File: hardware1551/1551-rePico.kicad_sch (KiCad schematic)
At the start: 25 parts, among them J1 0.96_I2C_OLED, J10 TCBM, J11 JTAG, J6 Conn_01x05, J8 SD CARD, U1 Pico, U3 XC9572XL-VQ64, U4 6523 (pins), U5 6510T (pins), U6 6510T (socket for chip)

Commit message: board for 1551 with correct dimensions and spacing between CPU and TPI, routed
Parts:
- C1, J1, J11, J8, SWDBG1, U1, U4, U5, U6: now left out of the parts list
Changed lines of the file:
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@@
 		(unit 1)
 		(exclude_from_sim no)
-		(in_bom yes)
+		(in_bom no)
 		(on_board yes)
 		(dnp no)
@@
 		(unit 1)
 		(exclude_from_sim no)
-		(in_bom yes)
+		(in_bom no)
 		(on_board yes)
 		(dnp no)
@@
 		(unit 1)
 		(exclude_from_sim no)
-		(in_bom yes)
+		(in_bom no)
 		(on_board yes)
 		(dnp no)
@@
 		(unit 1)
 		(exclude_from_sim no)
-		(in_bom yes)
+		(in_bom no)
 		(on_board yes)
 		(dnp no)
@@
 		(unit 1)
 		(exclude_from_sim no)
-		(in_bom yes)
+		(in_bom no)
 		(on_board yes)
 		(dnp no)
@@
 		(unit 1)
 		(exclude_from_sim no)
-		(in_bom yes)
+		(in_bom no)
 		(on_board yes)
 		(dnp no)
@@
 		(unit 1)
 		(exclude_from_sim no)
-		(in_bom yes)
+		(in_bom no)
 		(on_board yes)
 		(dnp no)
@@
 		(unit 1)
 		(exclude_from_sim no)
-		(in_bom yes)
+		(in_bom no)
 		(on_board yes)
 		(dnp no)
@@
 		(unit 1)
 		(exclude_from_sim no)
-		(in_bom yes)
+		(in_bom no)
 		(on_board yes)
 		(dnp no)

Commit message: jumpers for future GPIO0/GPIO3 experiments
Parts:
- added JP2, JP5, JP6, JP7: SolderJumper_3_Bridged12, Jumper:SolderJumper-3_P1.3mm_Bridged12_RoundedPad1.0x1.5mm_NumberLabels, symbol Jumper:SolderJumper_3_Bridged12
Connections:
- net +3V3: now also JP7.3 (B)
- net DEVNUM_3V3: now also JP5.2 (C); no longer U1.5 (GPIO3)
- net GND: now also JP7.1 (A)
- net PHI0: now also JP2.2 (C); no longer U5.2 (ϕ0)
- net ~{IRQ}: now also JP6.2 (C); no longer U5.3 (~{IRQ})
- net at U1.1 (GPIO0): now also JP2.3 (B)
- new net: JP5.1 (A), JP6.3 (B), U1.5 (GPIO3)
- new net: JP5.3 (B), JP7.2 (C)
- new net PHI0_BRD: JP2.1 (A), U5.2 (ϕ0)
- new net ~{IRQ_BRD}: JP6.1 (A), U5.3 (~{IRQ})
- no-connect marks 23 -> 22
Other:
- note added: "DEFAULT - use GPIO3 to drive DEVNUM_3V3 (Pico sets device number) - IRQ comes from the board OR - swap both JP5/JP6 - IRQ comes from GPIO3 - DEVNUM_3V3 set by JP7: GND (default) is #8, +3V3 is #9"
- note added: "Pico firmware TODO: - GPIO0: SOE not used (always high), can be fixed in firmware to true OR can be used to test 2MHz clock (PHI0) for 6502 - GPIO3: Pico decides about device number - 0 or 1 OR can be used to test 100Hz (IRQ) for 6502 - GPIO5: switch driver from high/low to hi-z/low"
- note removed: "Pico firmware TODO: - GPIO0: SOE not used (always high), can be fixed in firmware to true - GPIO3: Pico decides about device number - 0 or 1 - GPIO5: switch driver from high/low to hi-z/low"

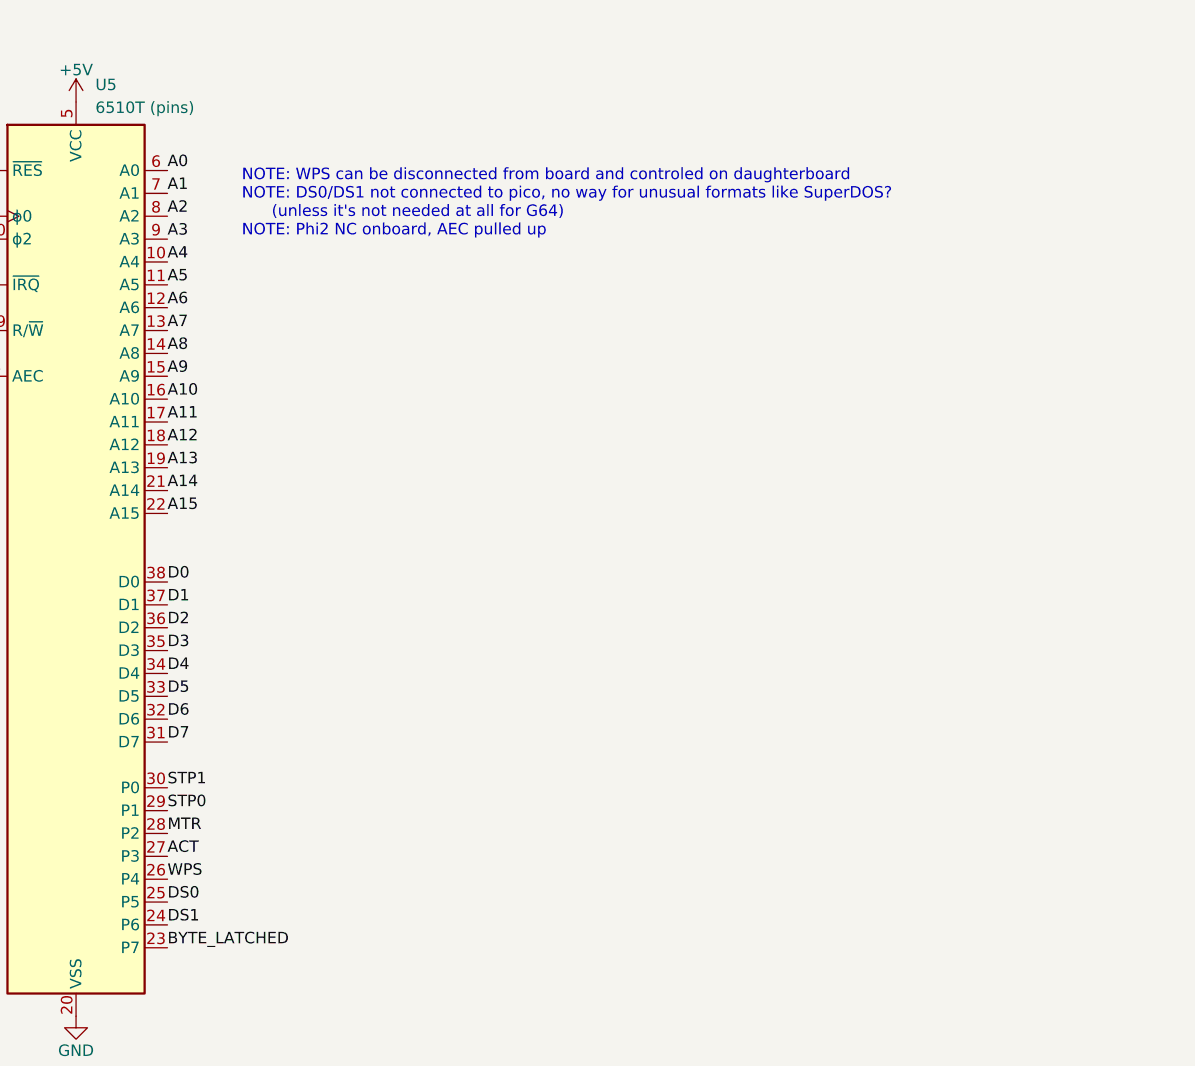
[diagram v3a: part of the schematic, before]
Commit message: disconnect WPS from mainboard WPS becuase it's an output of U8 (pin2) that will keep it low with no mechanism present
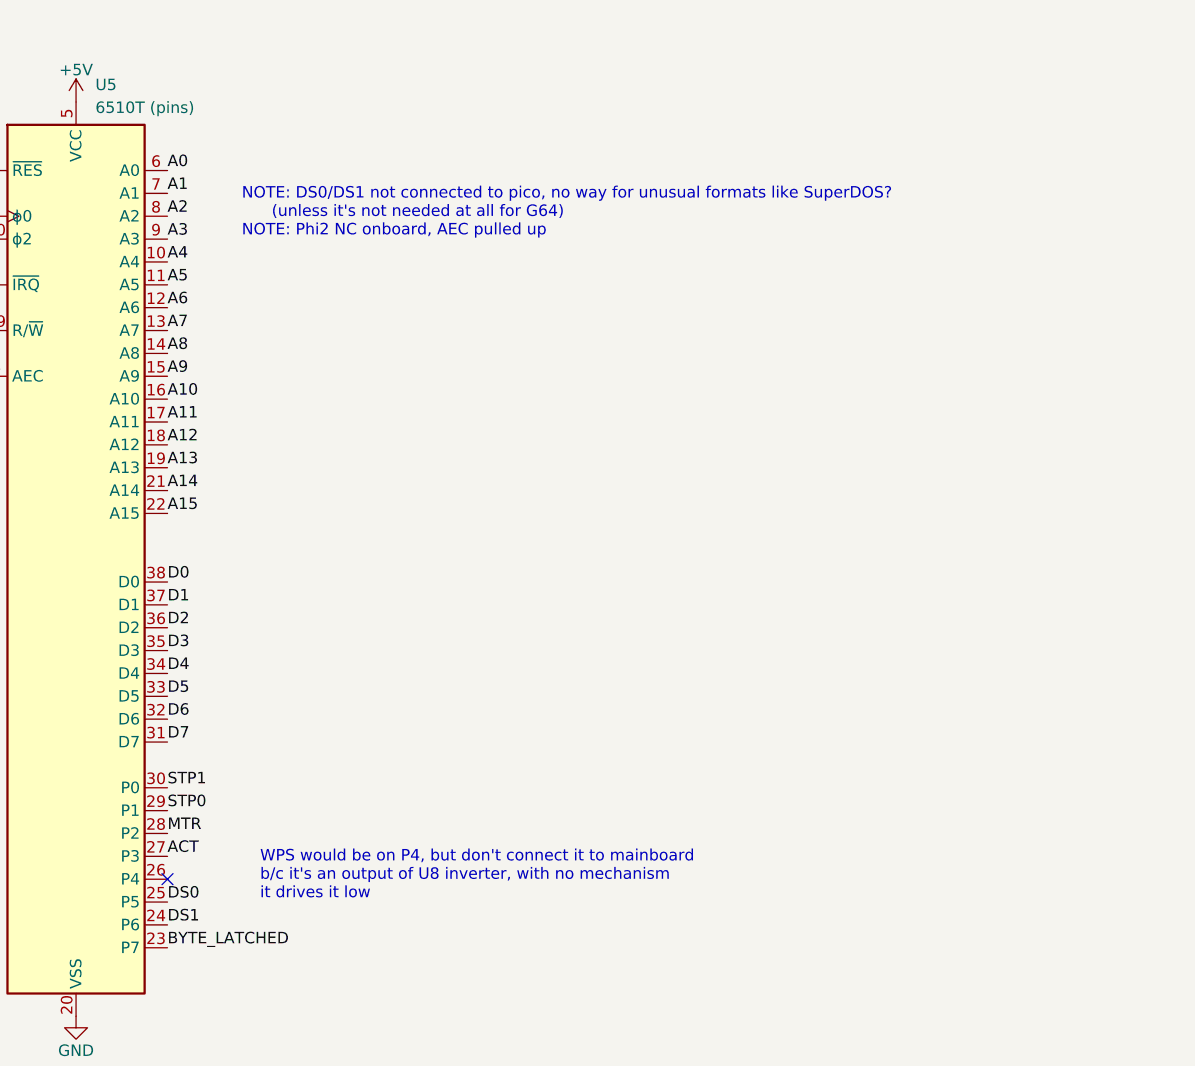
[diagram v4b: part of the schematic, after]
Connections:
- net WPS: no longer U5.26 (P4)
- no-connect marks 22 -> 23
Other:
- note added: "NOTE: DS0/DS1 not connected to pico, no way for unusual formats like SuperDOS? (unless it's not needed at all for G64) NOTE: Phi2 NC onboard, AEC pulled up"
- note added: "WPS would be on P4, but don't connect it to mainboard b/c it's an output of U8 inverter, with no mechanism it drives it low"
- note removed: "NOTE: WPS can be disconnected from board and controled on daughterboard NOTE: DS0/DS1 not connected to pico, no way for unusual formats like SuperDOS? (unless it's not needed at all for G64) NOTE: Phi2 NC onboard, AEC pulled up"
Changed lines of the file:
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@@
 		)
 	)
-	(text "NOTE: WPS can be disconnected from board and controled on daughterboard\nNOTE: DS0/DS1 not connected to pico, no way for unusual formats like SuperDOS?\n      (unless it's not needed at all for G64)\nNOTE: Phi2 NC onboard, AEC pulled up"
+	(text "NOTE: DS0/DS1 not connected to pico, no way for unusual formats like SuperDOS?\n      (unless it's not needed at all for G64)\nNOTE: Phi2 NC onboard, AEC pulled up"
 		(exclude_from_sim no)
 		(at 353.06 121.158 0)
@@
 		)
 	)
+	(text "WPS would be on P4, but don't connect it to mainboard\nb/c it's an output of U8 inverter, with no mechanism\nit drives it low"
+		(exclude_from_sim no)
+		(at 355.092 192.024 0)
+		(effects
+			(font
+				(size 1.27 1.27)
+			)
+			(justify left)
+		)
+	)
 	(text "Pico firmware TODO:\n- GPIO0: SOE not used (always high), can be fixed in firmware to true\n  OR can be used to test 2MHz clock (PHI0) for 6502\n- GPIO3: Pico decides about device number - 0 or 1\n  OR can be used to test 100Hz (IRQ) for 6502\n- GPIO5: switch driver from high/low to hi-z/low"
 		(exclude_from_sim no)
@@
 	)
 	(no_connect
+		(at 344.805 192.405)
+	)
+	(no_connect
 		(at 384.175 71.755)
 	)
@@
 		(effects
 			(font
-				(size 1.27 1.27)
-			)
-			(justify left bottom)
-		)
-	)
-	(label "WPS"
-		(at 344.805 192.405 0)
-		(effects
-			(font

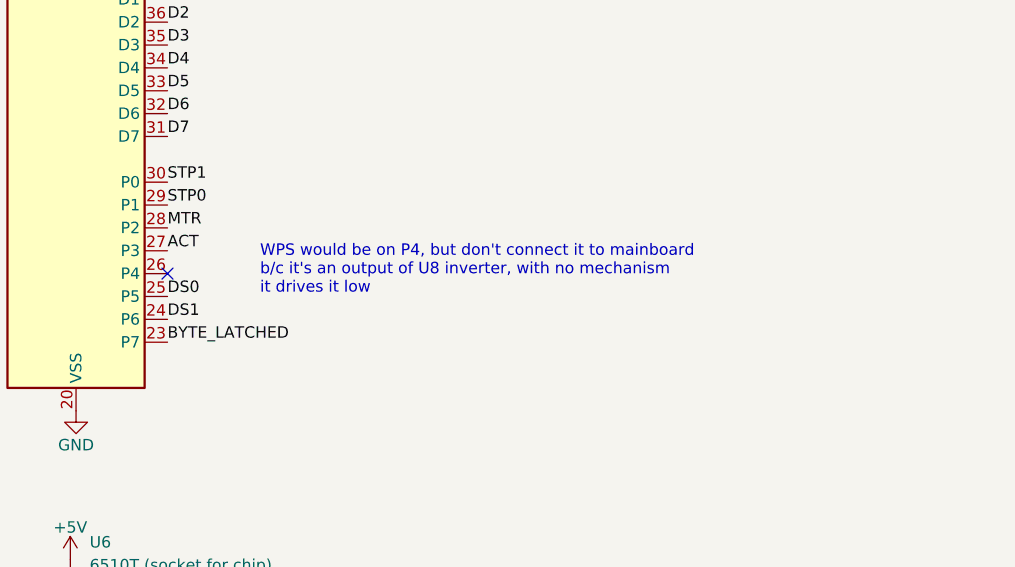
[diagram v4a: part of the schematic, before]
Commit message: remove BYTE_LATCHED connection to the board, keep it only between CPU and CPLD
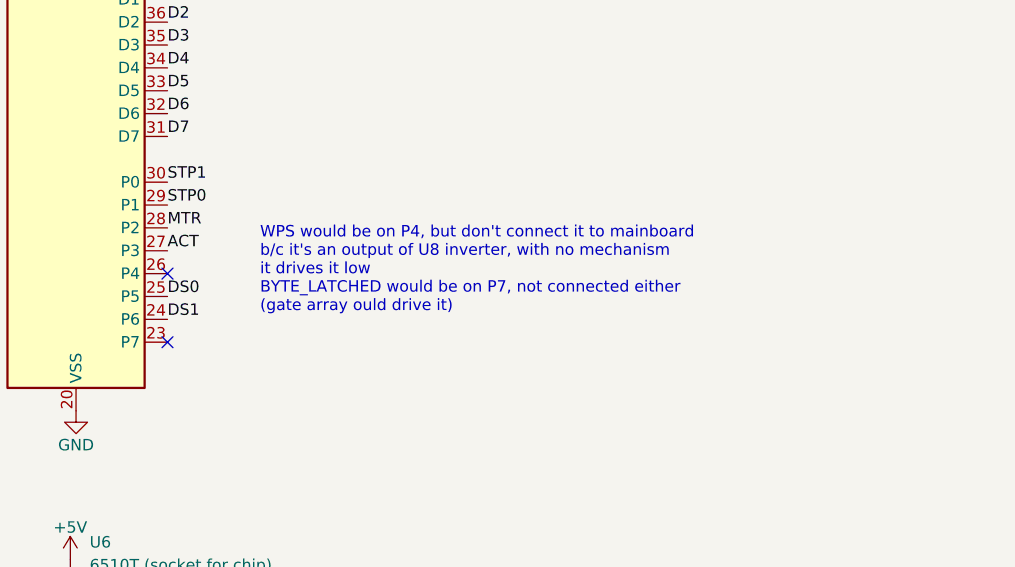
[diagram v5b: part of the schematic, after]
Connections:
- net BYTE_LATCHED: no longer U5.23 (P7)
- no-connect marks 23 -> 24
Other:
- note added: "WPS would be on P4, but don't connect it to mainboard b/c it's an output of U8 inverter, with no mechanism it drives it low BYTE_LATCHED would be on P7, not connected either (gate array ould drive it)"
- note removed: "WPS would be on P4, but don't connect it to mainboard b/c it's an output of U8 inverter, with no mechanism it drives it low"
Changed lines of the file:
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@@
 		)
 	)
-	(text "WPS would be on P4, but don't connect it to mainboard\nb/c it's an output of U8 inverter, with no mechanism\nit drives it low"
+	(text "WPS would be on P4, but don't connect it to mainboard\nb/c it's an output of U8 inverter, with no mechanism\nit drives it low\nBYTE_LATCHED would be on P7, not connected either\n(gate array ould drive it)"
 		(exclude_from_sim no)
 		(at 355.092 192.024 0)
@@
 	)
 	(no_connect
+		(at 344.805 200.025)
+	)
+	(no_connect
 		(at 529.59 65.405)
 	)
@@
 		(effects
 			(font
-				(size 1.27 1.27)
-			)
-			(justify left bottom)
-		)
-	)
-	(label "BYTE_LATCHED"
-		(at 344.805 200.025 0)
-		(effects
-			(font
